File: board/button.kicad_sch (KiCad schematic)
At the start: 4 parts, among them SW1 SW_Push, U1 PCF8574

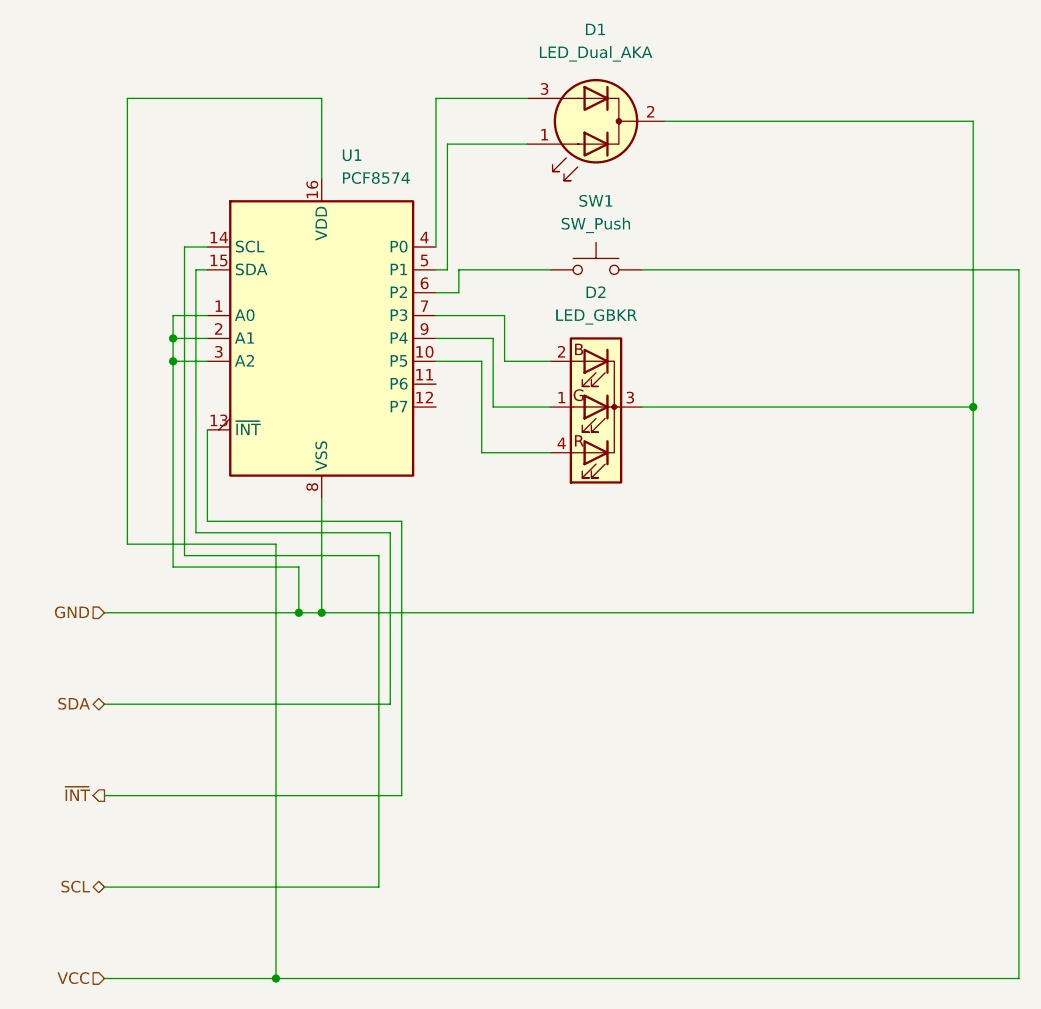
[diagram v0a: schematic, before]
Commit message: Creating PCB for 'THE BUTTON'
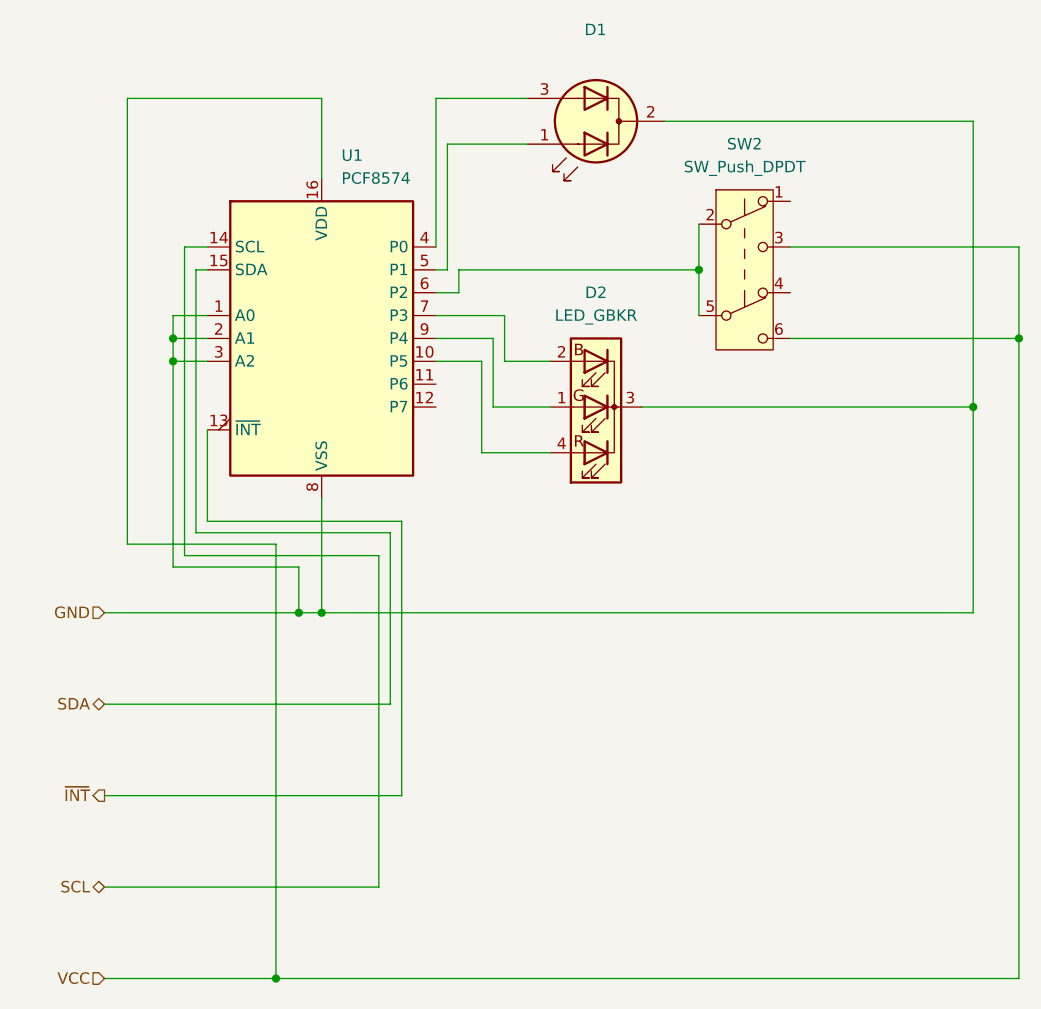
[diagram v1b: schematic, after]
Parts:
- removed SW1: SW_Push, symbol Switch:SW_Push
- added SW2: SW_Push_DPDT, Button_Switch_THT:SW_Push_2P2T_Toggle_CK_PVA2xxH1xxxxxxV2, symbol Switch:SW_Push_DPDT
- D1: footprint (none) -> LED_THT:LED_D8.0mm-3
- D2: footprint (none) -> LED_THT:LED_D5.0mm-4_RGB
- U1: footprint (none) -> PCM_Package_SO_AKL:SOIC-16W_7.5x10.3mm_P1.27mm
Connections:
- net VCC: now also SW2.3 (C), SW2.6 (C)
- net at U1.6 (P2): now also SW2.2 (B), SW2.5 (B)
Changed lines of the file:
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@@
+	)
+	(junction
+		(at 133.35 54.61)
+		(diameter 0)
+		(color 0 0 0 0)
+	)
+	(junction
+		(at 97.79 46.99)
+		(diameter 0)
+		(color 0 0 0 0)
 	)
 	(junction
@@
 	(wire
 		(pts
-			(xy 133.35 46.99) (xy 133.35 125.73)
+			(xy 133.35 44.45) (xy 133.35 54.61)
+		)
+		(stroke
+			(width 0)
+			(type default)
+		)
+	)
+	(wire
+		(pts
+			(xy 97.79 41.91) (xy 97.79 46.99)
 		)
 		(stroke
@@
 	(wire
 		(pts
-			(xy 71.12 46.99) (xy 81.28 46.99)
+			(xy 71.12 46.99) (xy 97.79 46.99)
 		)
 		(stroke
@@
 	(wire
 		(pts
+			(xy 107.95 54.61) (xy 133.35 54.61)
+		)
+		(stroke
+			(width 0)
+			(type default)
+		)
+	)
+	(wire
+		(pts
+			(xy 107.95 44.45) (xy 133.35 44.45)
+		)
+		(stroke
+			(width 0)
+			(type default)
+		)
+	)
+	(wire
+		(pts
 			(xy 76.2 52.07) (xy 76.2 57.15)
 		)
@@
 	(wire
 		(pts
-			(xy 91.44 46.99) (xy 133.35 46.99)
-		)
-		(stroke
-			(width 0)
-			(type default)
-		)
-	)
-	(wire
-		(pts
 			(xy 39.37 57.15) (xy 43.18 57.15)
 		)
@@
 	(wire
 		(pts
+			(xy 133.35 54.61) (xy 133.35 125.73)
+		)
+		(stroke
+			(width 0)
+			(type default)
+		)
+	)
+	(wire
+		(pts
 			(xy 50.8 77.47) (xy 34.29 77.47)
 		)
@@
 		(pts
 			(xy 68.58 27.94) (xy 78.74 27.94)
+		)
+		(stroke
+			(width 0)
+			(type default)
+		)
+	)
+	(wire
+		(pts
+			(xy 97.79 46.99) (xy 97.79 52.07)
 		)
 		(stroke
@@
 					(size 1.27 1.27)
 				)
-			)
-		)
-		(property "Footprint" ""
+				(hide yes)
+			)
+		)
+		(property "Footprint" "LED_THT:LED_D8.0mm-3"
 			(at 86.36 30.48 0)
 			(effects
@@
 				(path "/b5a6c315-00b5-445d-a49f-bfda9e5399e4/569f2921-3a89-4e88-a759-21a99ccb92c0"
 					(reference "D1")
+					(unit 1)
+				)
+			)
+		)
+	)
+	(symbol
+		(lib_id "Switch:SW_Push_DPDT")
+		(at 102.87 46.99 0)
+		(unit 1)
+		(exclude_from_sim no)
+		(in_bom yes)
+		(on_board yes)
+		(dnp no)
+		(fields_autoplaced yes)
+		(property "Reference" "SW2"
+			(at 102.87 33.02 0)
+			(effects
+				(font
+					(size 1.27 1.27)
+				)
+			)
+		)
+		(property "Value" "SW_Push_DPDT"
+			(at 102.87 35.56 0)
+			(effects
+				(font
+					(size 1.27 1.27)
+				)
+			)
+		)
+		(property "Footprint" "Button_Switch_THT:SW_Push_2P2T_Toggle_CK_PVA2xxH1xxxxxxV2"
+			(at 102.87 41.91 0)
+			(effects
+				(font
+					(size 1.27 1.27)
+				)
+				(hide yes)
+			)
+		)
+		(property "Datasheet" "~"
+			(at 102.87 41.91 0)
+			(effects
+				(font
+					(size 1.27 1.27)
+				)
+				(hide yes)
+			)
+		)
+		(property "Description" "Momentary Switch, dual pole double throw"
+			(at 102.87 46.99 0)
+			(effects
+				(font
+					(size 1.27 1.27)
+				)
+				(hide yes)
+			)
+		)
+		(pin "5"
+		)
+		(pin "1"
+		)
+		(pin "4"
+		)
+		(pin "3"
+		)
+		(pin "2"
+		)
+		(pin "6"
+		)
+		(instances
+			(project "board"
+				(path "/b5a6c315-00b5-445d-a49f-bfda9e5399e4/569f2921-3a89-4e88-a759-21a99ccb92c0"
+					(reference "SW2")
 					(unit 1)
 				)
@@
 			)
 		)
-		(property "Footprint" ""
+		(property "Footprint" "LED_THT:LED_D5.0mm-4_RGB"
 			(at 86.36 60.96 0)
 			(effects
@@
 			)
 		)
-		(property "Footprint" ""
+		(property "Footprint" "PCM_Package_SO_AKL:SOIC-16W_7.5x10.3mm_P1.27mm"
 			(at 55.88 54.61 0)
 			(effects
@@
 					(unit 1)
 				)
-			)
-		)
-	)
-	(symbol
-		(lib_id "Switch:SW_Push")
-		(at 86.36 46.99 0)
-		(unit 1)
-		(exclude_from_sim no)
-		(in_bom yes)
-		(on_board yes)
-		(dnp no)
-		(fields_autoplaced yes)
-		(property "Reference" "SW1"
-			(at 86.36 39.37 0)
-			(effects
-				(font
-					(size 1.27 1.27)
-				)
-			)
-		)
-		(property "Value" "SW_Push"
-			(at 86.36 41.91 0)
-			(effects
-				(font
-					(size 1.27 1.27)
-				)
-			)
-		)
-		(property "Footprint" ""
-			(at 86.36 41.91 0)
-			(effects
-				(font
-					(size 1.27 1.27)
-				)
-				(hide yes)
-			)
-		)
-		(property "Datasheet" "~"
-			(at 86.36 41.91 0)
-			(effects
-				(font
-					(size 1.27 1.27)
-				)
-				(hide yes)
-			)
-		)
-		(property "Description" "Push button switch, generic, two pins"
-			(at 86.36 46.99 0)
-			(effects
-				(font
-					(size 1.27 1.27)
-				)
-				(hide yes)
-			)
-		)
-		(pin "2"
-		)
-		(pin "1"
-		)
-		(instances
-			(project "board"
-				(path "/b5a6c315-00b5-445d-a49f-bfda9e5399e4/569f2921-3a89-4e88-a759-21a99ccb92c0"
-					(reference "SW1")
-					(unit 1)
-				)
